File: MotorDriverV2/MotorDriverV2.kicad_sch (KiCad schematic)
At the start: 16 parts, among them IC1 TC78H620FNG, IC2 ESP32-C3FH4X, J1 Power, J2 Input, J3 Out_A, J4 Out_B

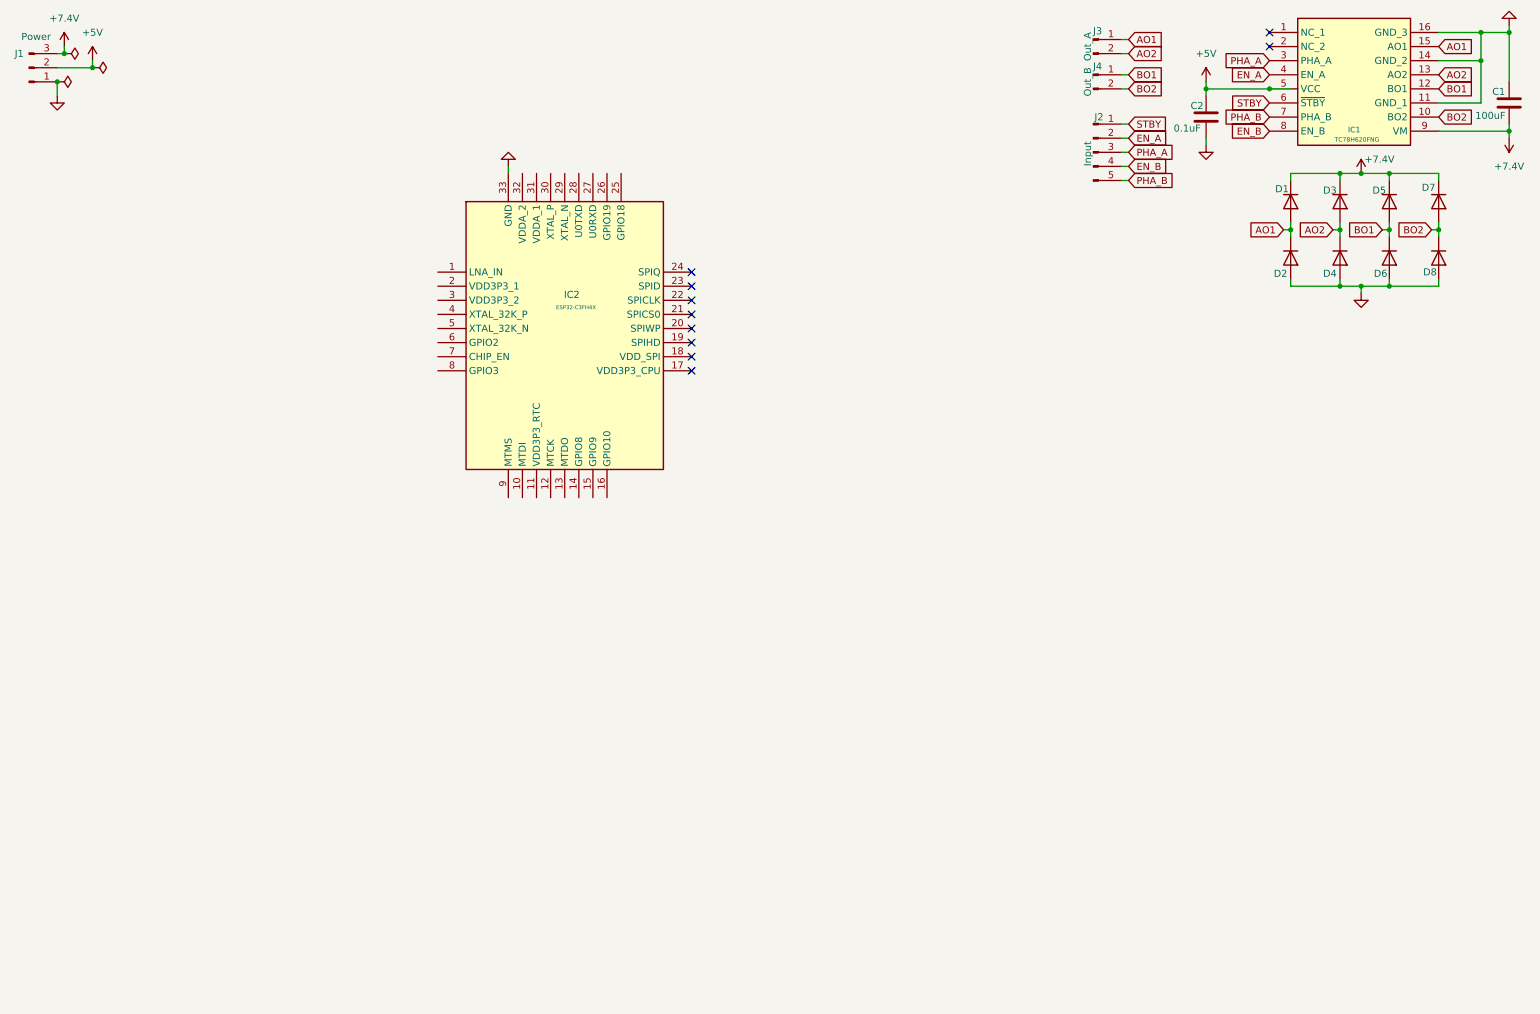
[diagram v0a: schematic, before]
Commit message: UPDATE: Added symbols, fotprints and datasheets for components
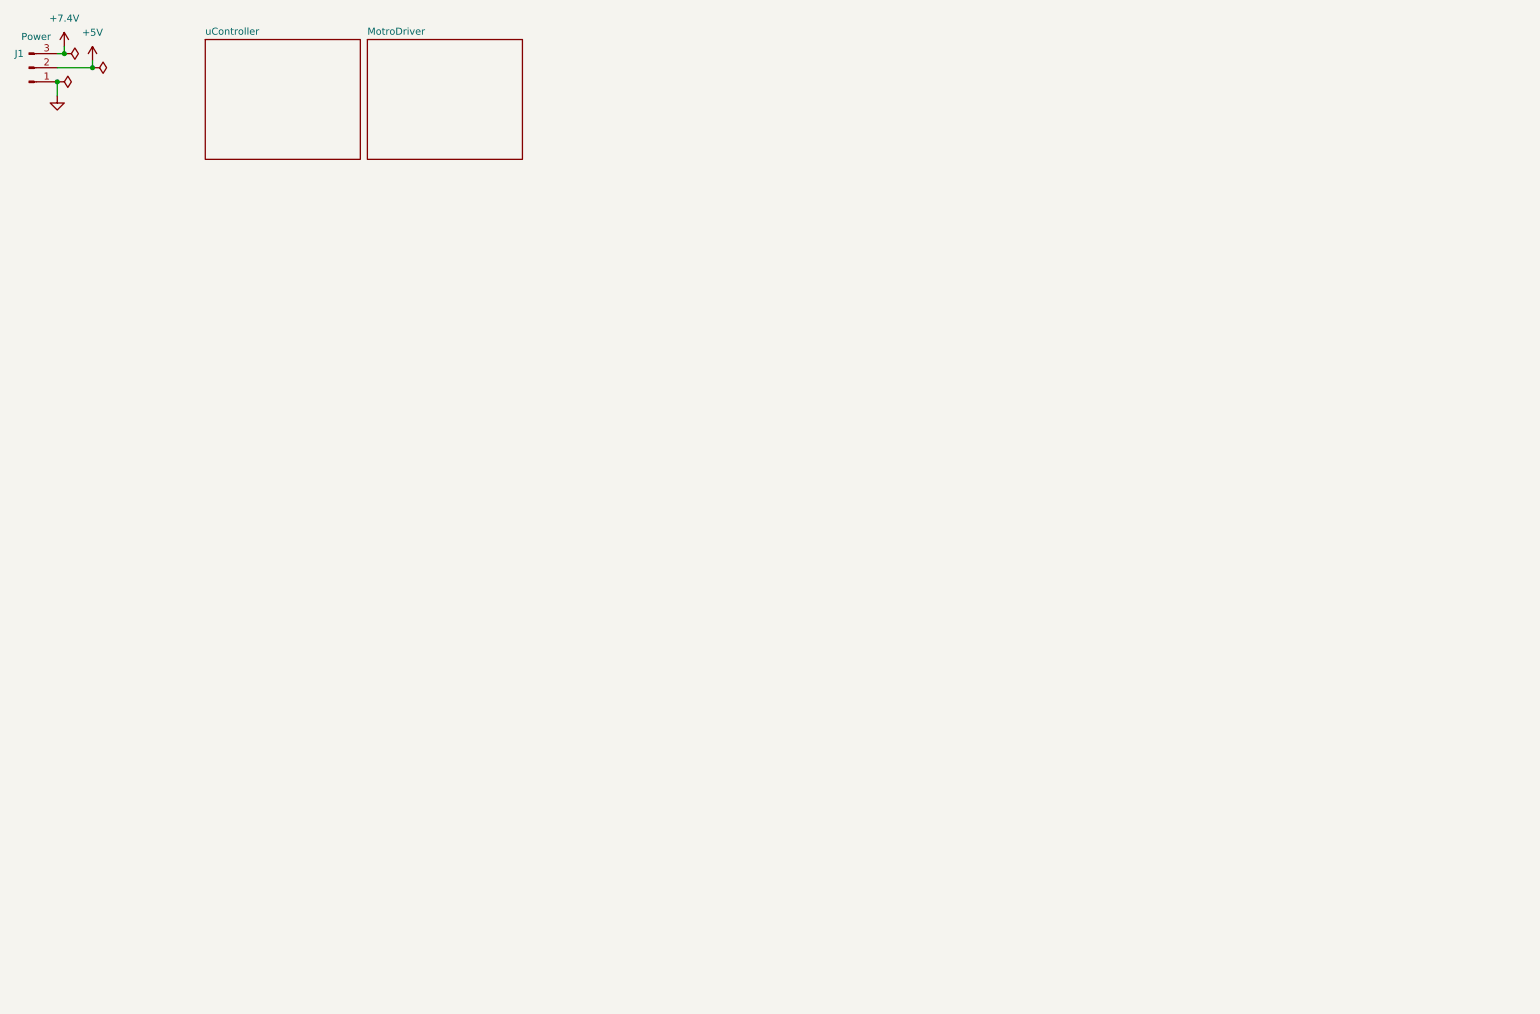
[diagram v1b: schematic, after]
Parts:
- removed C1: 100uF, Capacitor_SMD:C_0805_2012Metric_Pad1.18x1.45mm_HandSolder, symbol Device:C
- removed C2: 0.1uF, Capacitor_SMD:C_0805_2012Metric_Pad1.18x1.45mm_HandSolder, symbol Device:C
- removed D1, D2, D3, D4, D5, D6, D7, D8: 1N4001, Diode_THT:D_DO-41_SOD81_P10.16mm_Horizontal, symbol Diode:1N4001
- removed IC1: TC78H620FNG, TC78H620FNG:SOP65P640X160-16N, symbol TC78H620FNG:TC78H620FNG
- removed IC2: ESP32-C3FH4X, ESP32-C3FH4X:QFN50P500X500X90-33N-D, symbol ESP32-C3FH4X:ESP32-C3FH4X
- removed J2: Input, Connector_PinHeader_2.54mm:PinHeader_1x05_P2.54mm_Vertical, symbol Connector:Conn_01x05_Pin
- removed J3: Out_A, Connector_JST:JST_XH_B2B-XH-A_1x02_P2.50mm_Vertical, symbol Connector:Conn_01x02_Pin
- removed J4: Out_B, Connector_JST:JST_XH_B2B-XH-A_1x02_P2.50mm_Vertical, symbol Connector:Conn_01x02_Pin
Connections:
- no-connect marks 10 -> 0
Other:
- added sheet MotroDriver (MotorDriver_sch.kicad_sch)
- added sheet uController (uController_sch.kicad_sch)

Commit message: UPDATE: Schematic
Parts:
- added C1, C6: 0.1uF, Capacitor_SMD:C_0805_2012Metric_Pad1.18x1.45mm_HandSolder, symbol Device:C
- added C10, C11, C13, C4, C9: 0.1uF, symbol Device:C
- added C12, C3, C8: 10uF, symbol Device:C
- added C2, C7: 47uF, Capacitor_SMD:C_0805_2012Metric_Pad1.18x1.45mm_HandSolder, symbol Device:C
- added C5: 1uF, symbol Device:C
- added D1: LED, LED_SMD:LED_0805_2012Metric_Pad1.15x1.40mm_HandSolder, symbol Device:LED
- added IC1, IC2: DRV8871DDARQ1, DRV8871DDARQ1:SOIC127P600X170-9N, symbol DRV8871DDARQ1:DRV8871DDARQ1
- added IC3: ESP32-S3-WROOM-1U-N4, ESP32-S3-WROOM-1U-N4:ESP32S3WROOM1UN4, symbol ESP32-S3-WROOM-1U-N4:ESP32-S3-WROOM-1U-N4
- added J2: Out_A, Connector_JST:JST_XH_B2B-XH-A_1x02_P2.50mm_Vertical, symbol Connector:Conn_01x02_Pin
- added J3: Conn_01x10_Pin, Connector_PinHeader_2.54mm:PinHeader_1x10_P2.54mm_Vertical, symbol Connector:Conn_01x10_Pin
- added J4: Out_B, Connector_JST:JST_XH_B2B-XH-A_1x02_P2.50mm_Vertical, symbol Connector:Conn_01x02_Pin
- added J5: USB_C_Receptacle_USB2.0_14P, symbol Connector:USB_C_Receptacle_USB2.0_14P
- added PS1: LM1117IMPX-3.3_NOPB, SOT230P700X180-4N, symbol LM1117IMPX-3_3_NOPB:LM1117IMPX-3.3_NOPB
- added R1, R2: 14.8K, Resistor_THT:R_Axial_DIN0207_L6.3mm_D2.5mm_P7.62mm_Horizontal, symbol Device:R
- added R3: 10k, Resistor_THT:R_Axial_DIN0207_L6.3mm_D2.5mm_P7.62mm_Horizontal, symbol Device:R
- added R4, R5, R6: 5k1, Resistor_THT:R_Axial_DIN0207_L6.3mm_D2.5mm_P7.62mm_Horizontal, symbol Device:R
- added S1, S2: PTS636SKG25JSMTR_LFS, PTS636SKG25JSMTR_LFS:PTS636SKG25JSMTRLFS, symbol PTS636SKG25JSMTR_LFS:PTS636SKG25JSMTR_LFS
- added U1: USBLC6-2SC6, Package_TO_SOT_SMD:SOT-23-6, symbol Power_Protection:USBLC6-2SC6
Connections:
- net +5V: now also C8.1, C9.1, J5.A4 (VBUS), J5.A9 (VBUS), J5.B4 (VBUS), J5.B9 (VBUS), PS1.3 (INPUT), U1.5 (VBUS)
- net +7.4V: now also C1.1, C2.1, C6.1, C7.1, IC1.5 (VM), IC2.5 (VM)
- net GND: now also C1.2, C10.1, C11.2, C12.2, C13.1, C2.2, C3.2, C4.2, C5.2, C6.2, C7.2, C8.2, C9.2, D1.1 (K), IC1.1 (GND_1), IC1.7 (PGND), IC1.9 (GND_2), IC2.1 (GND_1), IC2.7 (PGND), IC2.9 (GND_2), IC3.1 (GND_1), IC3.40 (GND_2), IC3.41 (GND_3), IC3.42 (GND_4), IC3.43 (GND_5), IC3.44 (GND_6), IC3.45 (GND_7), IC3.46 (GND_8), IC3.47 (GND_9), IC3.48 (GND_10), IC3.49 (GND_11), J3.1 (Pin_1), J5.A1 (GND), J5.A12 (GND), J5.B1 (GND), J5.B12 (GND), J5.S1 (SHIELD), PS1.1 (ADJ/GND), R1.2, R2.2, R4.2, R5.2, S1.1 (COM), S1.3 (GND_1), S1.4 (GND_2), S2.1 (COM), S2.3 (GND_1), S2.4 (GND_2), U1.2 (GND)
- new net: IC2.4 (ILIM), R2.1
- new net: C5.1, R3.2
- new net: D1.2 (A), R6.2
- new net: J5.A5 (CC1), R4.1
- new net: J5.B5 (CC2), R5.1
- new net: J5.A7 (D-), J5.B7 (D-), U1.1 (I/O1)
- new net: J5.A6 (D+), J5.B6 (D+), U1.3 (I/O2)
- new net: IC1.4 (ILIM), R1.1
- new net +3V3: C11.1, C12.1, C3.1, C4.1, IC3.2 (3V3), J3.2 (Pin_2), PS1.2 (OUTPUT), PS1.4 (VOUT), R3.1, R6.1
- new net BOOT: C13.2, IC3.27 (IO0), S2.2 (NO)
- new net D+: U1.4 (I/O2)
- new net D-: U1.6 (I/O1)
- new net EN: C10.2, IC3.3 (EN), S1.2 (NO)
- new net IO_03: IC3.15 (IO3), J3.3 (Pin_3)
- new net IO_08: IC3.12 (IO8), J3.4 (Pin_4)
- new net IO_09: IC3.17 (IO9), J3.5 (Pin_5)
- new net IO_10: IC3.18 (IO10), J3.6 (Pin_6)
- new net IO_11: IC3.19 (IO11), J3.7 (Pin_7)
- new net IO_19: IC3.13 (IO19), J3.8 (Pin_8)
- new net IO_20: IC3.14 (IO20), J3.9 (Pin_9)
- new net IO_46: IC3.16 (IO46), J3.10 (Pin_10)
- new net In1_1: IC1.3 (IN1), IC3.7 (IO7)
- new net In1_2: IC1.2 (IN2), IC3.6 (IO6)
- new net In2_1: IC2.3 (IN1), IC3.4 (IO4)
- new net In2_2: IC2.2 (IN2), IC3.5 (IO5)
- new net Out1_1: IC1.6 (OUT1), J2.1 (Pin_1)
- new net Out1_2: IC1.8 (OUT2), J2.2 (Pin_2)
- new net Out2_1: IC2.6 (OUT1), J4.1 (Pin_1)
- new net Out2_2: IC2.8 (OUT2), J4.2 (Pin_2)
- no-connect marks 0 -> 23
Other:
- removed sheet MotroDriver
- removed sheet uController
- company: (none) -> Sinior Design - Team 04
- title: (none) -> Motor Driver

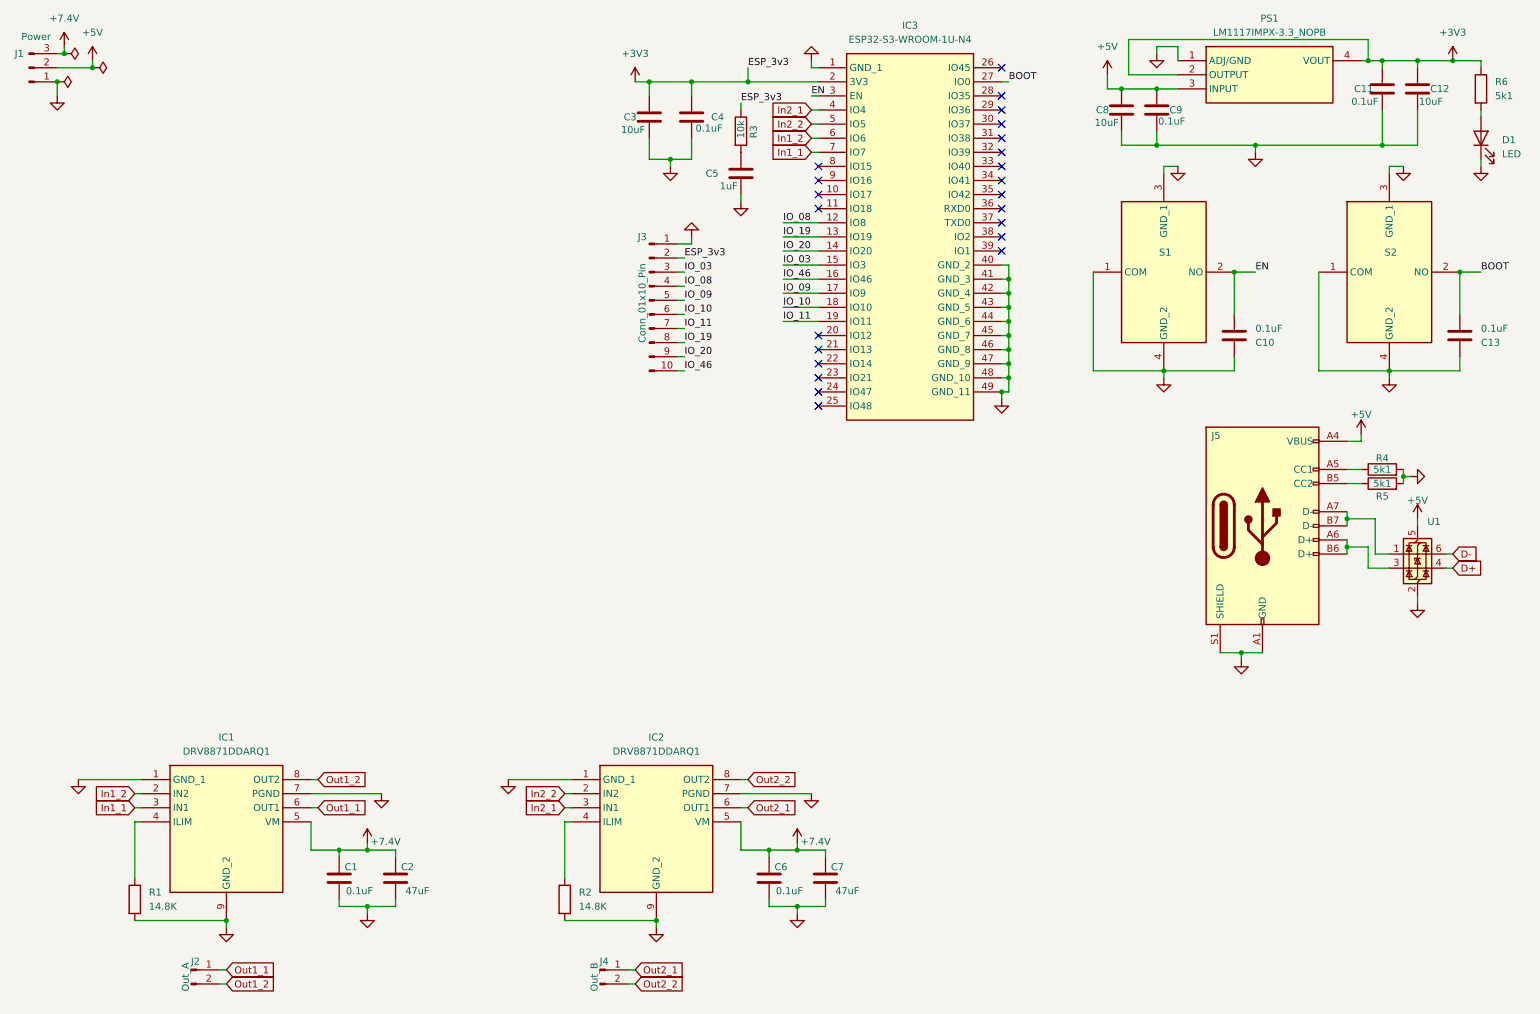
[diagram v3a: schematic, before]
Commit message: UPDATE: Symbols and footprint added, need to finish layout
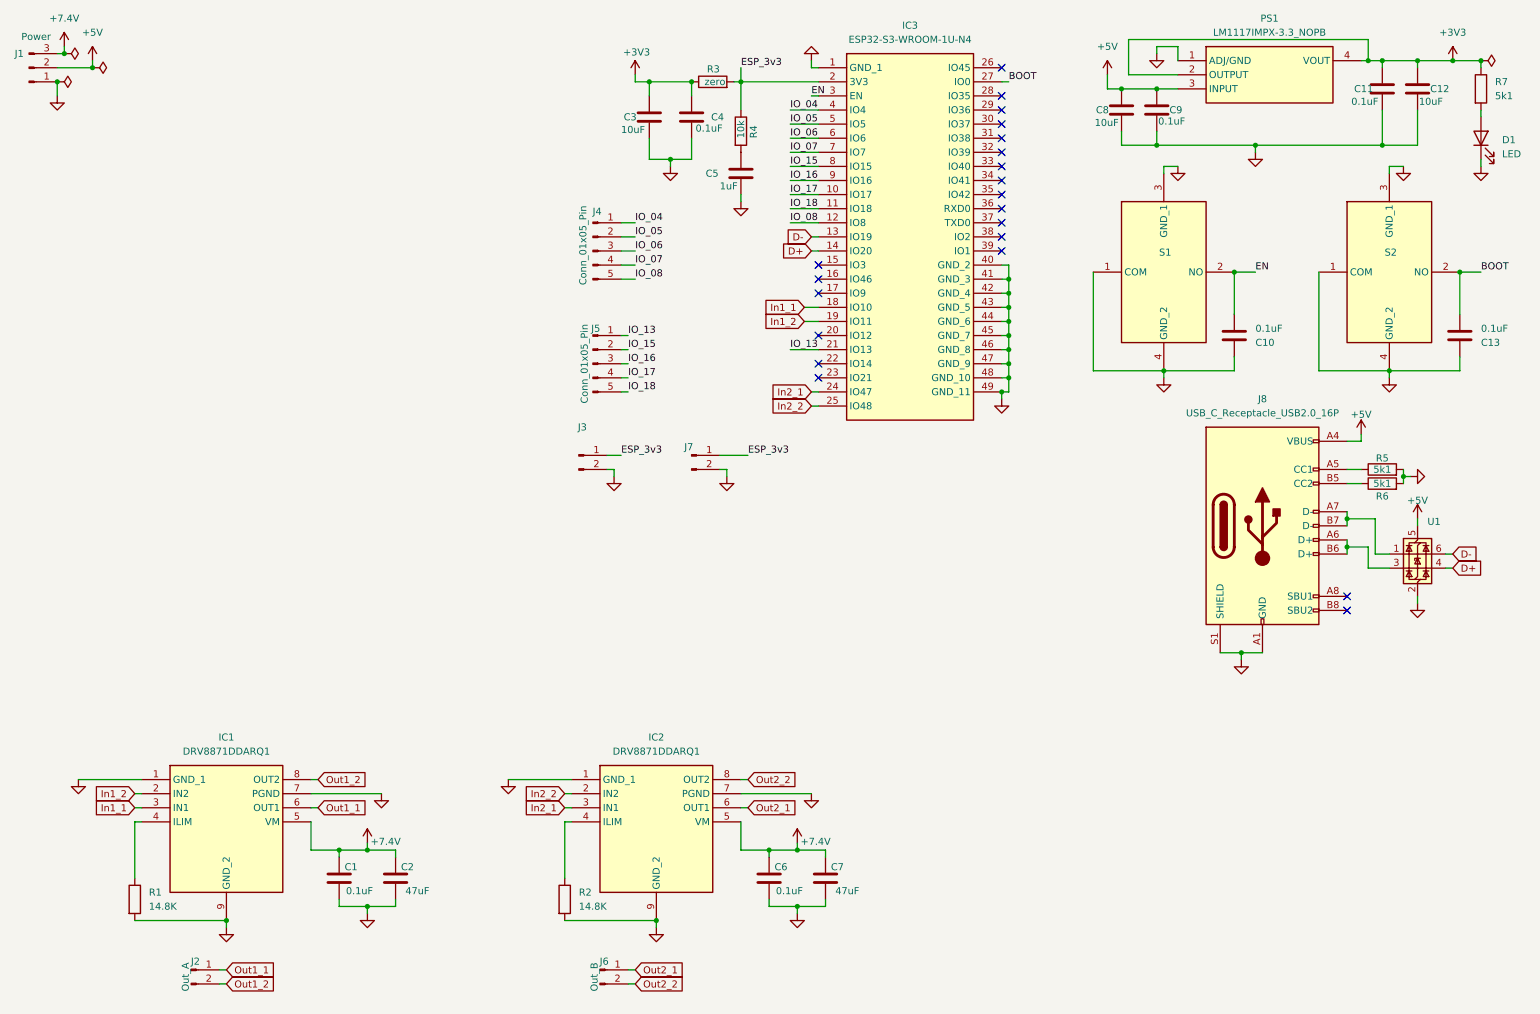
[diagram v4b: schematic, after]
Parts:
- removed J3: Conn_01x10_Pin, Connector_PinHeader_2.54mm:PinHeader_1x10_P2.54mm_Vertical, symbol Connector:Conn_01x10_Pin
- removed J5: USB_C_Receptacle_USB2.0_14P, symbol Connector:USB_C_Receptacle_USB2.0_14P
- added J3, J7: Conn_01x02_Pin, Connector_PinHeader_2.54mm:PinHeader_1x02_P2.54mm_Vertical, symbol Connector:Conn_01x02_Pin
- added J4, J5: Conn_01x05_Pin, Connector_PinHeader_2.54mm:PinHeader_1x05_P2.54mm_Vertical, symbol Connector:Conn_01x05_Pin
- added J8: USB_C_Receptacle_USB2.0_16P, Connector_USB:USB_C_Receptacle_GCT_USB4105-xx-A_16P_TopMnt_Horizontal, symbol Connector:USB_C_Receptacle_USB2.0_16P
- added R3: zero, Resistor_SMD:R_0805_2012Metric_Pad1.20x1.40mm_HandSolder, symbol Device:R
- C10, C11, C12, C13, C3, C4, C5, C8, C9: footprint (none) -> Capacitor_SMD:C_0805_2012Metric_Pad1.18x1.45mm_HandSolder
- PS1: footprint SOT230P700X180-4N -> LM1117IMPX-3.3:SOT230P700X180-4N
- R1, R2: footprint Resistor_THT:R_Axial_DIN0207_L6.3mm_D2.5mm_P7.62mm_Horizontal -> Resistor_SMD:R_0805_2012Metric_Pad1.20x1.40mm_HandSolder
- R4: renamed from R3; footprint Resistor_THT:R_Axial_DIN0207_L6.3mm_D2.5mm_P7.62mm_Horizontal -> Resistor_SMD:R_0805_2012Metric_Pad1.20x1.40mm_HandSolder
- R5: renamed from R4; footprint Resistor_THT:R_Axial_DIN0207_L6.3mm_D2.5mm_P7.62mm_Horizontal -> Resistor_SMD:R_0805_2012Metric_Pad1.20x1.40mm_HandSolder
- R6: renamed from R5; footprint Resistor_THT:R_Axial_DIN0207_L6.3mm_D2.5mm_P7.62mm_Horizontal -> Resistor_SMD:R_0805_2012Metric_Pad1.20x1.40mm_HandSolder
- R7: renamed from R6; footprint Resistor_THT:R_Axial_DIN0207_L6.3mm_D2.5mm_P7.62mm_Horizontal -> Resistor_SMD:R_0805_2012Metric_Pad1.20x1.40mm_HandSolder
- renumbered J4 to J6
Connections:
- net IO_10 is gone; now on net In1_1: IC3.18 (IO10)
- net IO_11 is gone; now on net In1_2: IC3.19 (IO11)
- net IO_19 is gone; now on net D-: IC3.13 (IO19)
- net IO_20 is gone; now on net D+: IC3.14 (IO20)
- net +3V3: now also R3.1; no longer IC3.2 (3V3), R4.1
- net +5V: now also J8.A4 (VBUS), J8.A9 (VBUS), J8.B4 (VBUS), J8.B9 (VBUS)
- net GND: now also J3.2 (Pin_2), J7.2 (Pin_2), J8.A1 (GND), J8.A12 (GND), J8.B1 (GND), J8.B12 (GND), J8.S1 (SHIELD)
- net IO_08: now also J4.5 (Pin_5)
- net In1_1: no longer IC3.7 (IO7)
- net In1_2: no longer IC3.6 (IO6)
- net In2_1: now also IC3.24 (IO47); no longer IC3.4 (IO4)
- net In2_2: now also IC3.25 (IO48); no longer IC3.5 (IO5)
- net at R5.1: now also J8.A5 (CC1)
- net IO_17: now reaches IC3.10 (IO17)
- net IO_17: now also J5.4 (Pin_4)
- net IO_18: now reaches IC3.11 (IO18)
- net IO_18: now also J5.5 (Pin_5)
- net IO_13: now reaches IC3.21 (IO13)
- net IO_13: now also J5.1 (Pin_1)
- net IO_15: now reaches IC3.8 (IO15)
- net IO_15: now also J5.2 (Pin_2)
- net IO_16: now reaches IC3.9 (IO16)
- net IO_16: now also J5.3 (Pin_3)
- net at R6.1: now also J8.B5 (CC2)
- net at U1.1 (I/O1): now also J8.A7 (D-), J8.B7 (D-)
- net at U1.3 (I/O2): now also J8.A6 (D+), J8.B6 (D+)
- net IO_03: no longer names the net of IC3.15 (IO3)
- net IO_09: no longer names the net of IC3.17 (IO9)
- net IO_46: no longer names the net of IC3.16 (IO46)
- new net ESP_3v3: IC3.2 (3V3), J3.1 (Pin_1), J7.1 (Pin_1), R3.2, R4.1
- new net IO_04: IC3.4 (IO4), J4.1 (Pin_1)
- new net IO_05: IC3.5 (IO5), J4.2 (Pin_2)
- new net IO_06: IC3.6 (IO6), J4.3 (Pin_3)
- new net IO_07: IC3.7 (IO7), J4.4 (Pin_4)
- no-connect marks 23 -> 21

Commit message: Final Update
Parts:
- IC1, IC2: value DRV8871DDARQ1 -> DRV8871
- J8: value USB_C_Receptacle_USB2.0_16P -> USB_C
- PS1: value LM1117IMPX-3.3_NOPB -> LM1117-3.3
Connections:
- net IO_13: now also J5.5 (Pin_5); no longer J5.1 (Pin_1)
- net IO_15: now also J5.1 (Pin_1); no longer J5.2 (Pin_2)
- net IO_16: now also J5.2 (Pin_2); no longer J5.3 (Pin_3)
- net IO_17: now also J5.3 (Pin_3); no longer J5.4 (Pin_4)
- net IO_18: now also J5.4 (Pin_4); no longer J5.5 (Pin_5)
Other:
- moved on the sheet: C1, C2, C6, C7, IC1, IC2, J1, J2, J6, R1, R2

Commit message: Completed PCB's
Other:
- moved on the sheet: C1, C10, C13, C2, C3, C4, C5, C6, C7, IC1, IC2, IC3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
